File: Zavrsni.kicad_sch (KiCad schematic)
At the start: 8 parts, among them J1 JOYSTICK, J2 LSM6DS3, J3 ILI9341, J4 NUCLEO-H743ZI2, J5 NUCLEO-H743ZI2, J6 NUCLEO-H743ZI2, J7 NUCLEO-H743ZI2, K1 JST-2pin-SMD

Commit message: Add files via upload
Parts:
- added C1: 100 nF, Capacitor_SMD:C_0603_1608Metric, symbol Device:C
- added C2, C3, C4, C5: C, Capacitor_SMD:C_0603_1608Metric, symbol Device:C
- added R1, R2, R3, R4, R5, R6: 10k, Resistor_SMD:R_0201_0603Metric, symbol Device:R
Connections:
- net +3V3: now also C1.1, C2.2, C3.2, C4.1, C5.1
- net CS: now also R4.1; no longer J3.3 (Pin_3)
- net GND: now also C1.2, C2.1, C3.1, C4.2, C5.2
- net SCK: now also R1.1; no longer J3.7 (Pin_7)
- net SDI: now also R2.1; no longer J3.6 (Pin_6)
- net SDO(MISO): now also R3.1; no longer J3.9 (Pin_9)
- new net: J3.7 (Pin_7), R1.2
- new net: J3.6 (Pin_6), R2.2
- new net: J3.3 (Pin_3), R4.2
- new net: J3.9 (Pin_9), R3.2
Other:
- moved on the sheet: J3

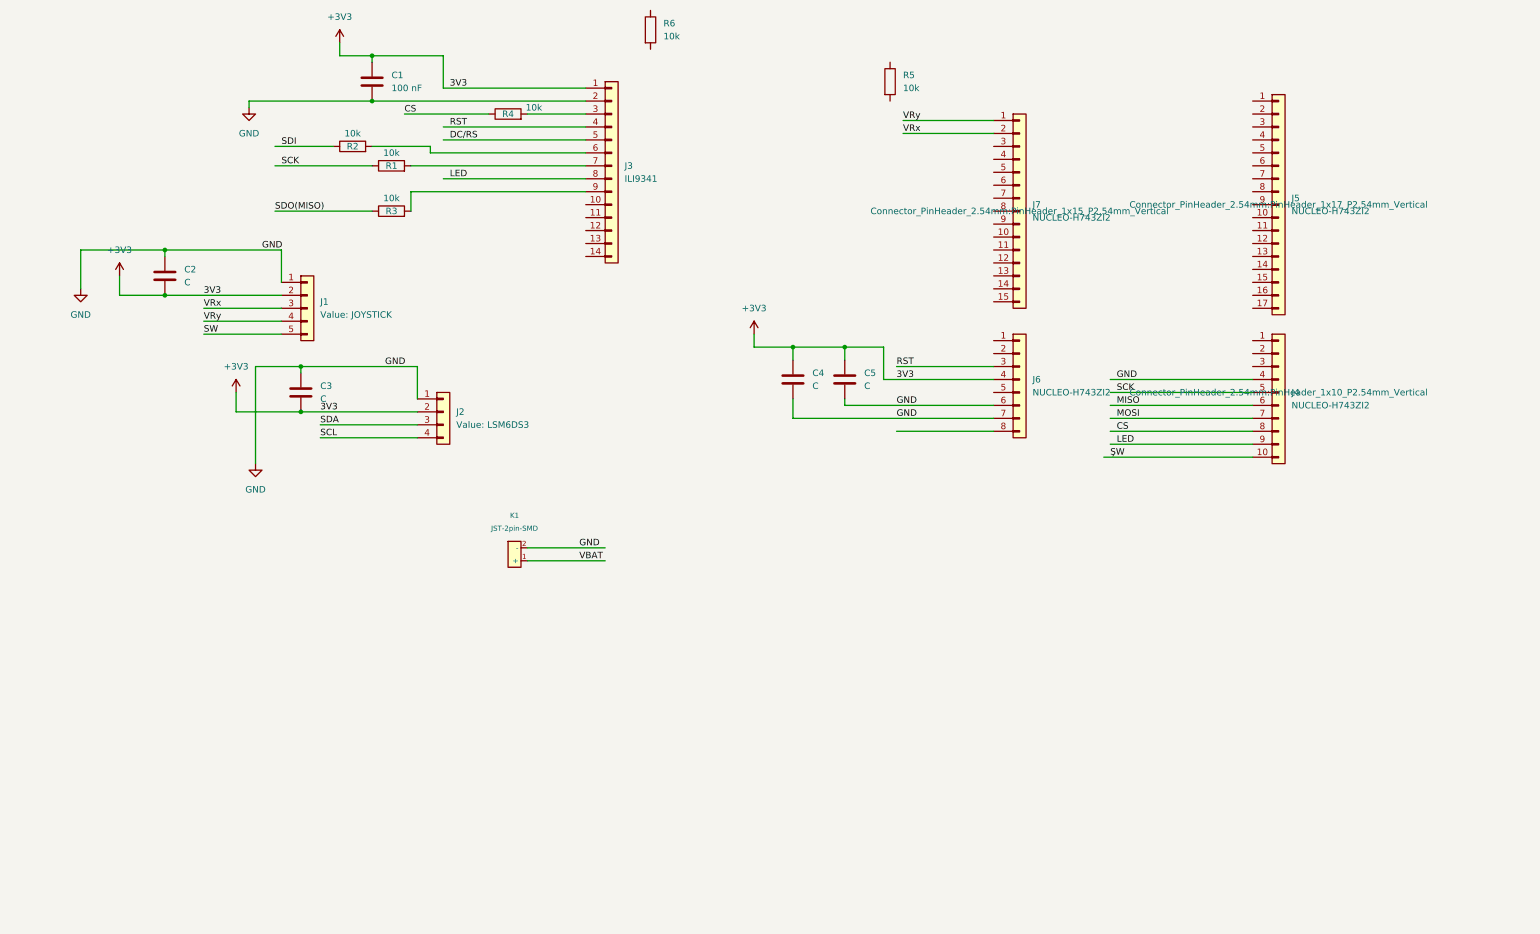
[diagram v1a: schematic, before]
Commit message: Added push buttons, and footprint for JST connector
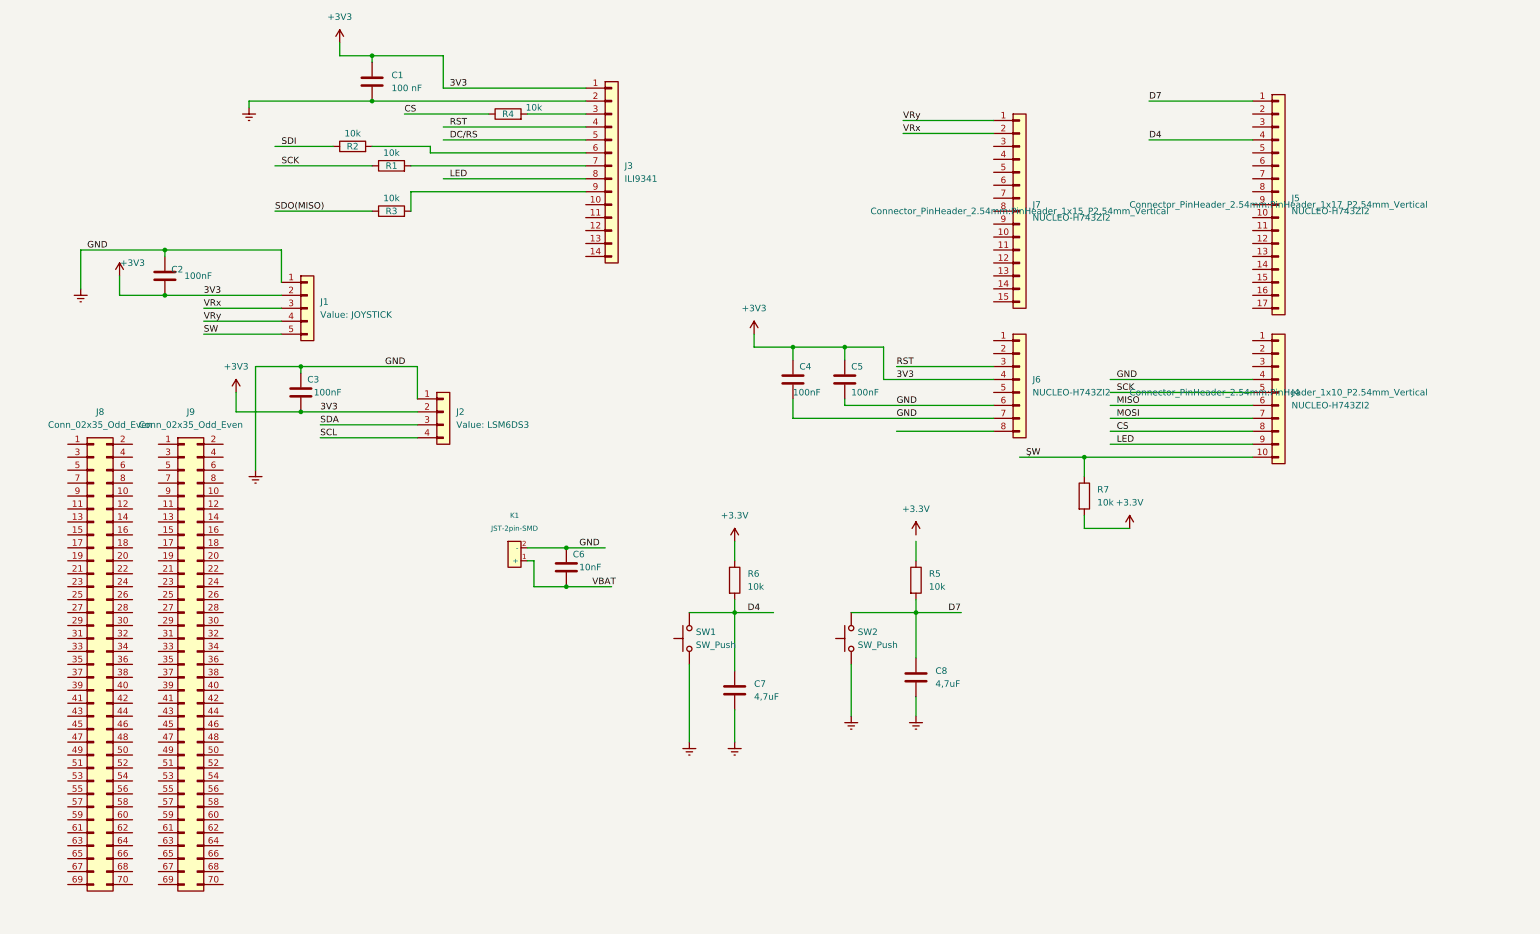
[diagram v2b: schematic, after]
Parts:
- added C6: 10nF, Capacitor_SMD:C_0603_1608Metric, symbol Device:C
- added C7, C8: 4,7uF, Capacitor_SMD:C_0603_1608Metric, symbol Device:C
- added J8, J9: Conn_02x35_Odd_Even, Connector_PinHeader_2.54mm:PinHeader_2x35_P2.54mm_Vertical, symbol Connector_Generic:Conn_02x35_Odd_Even
- added R7: 10k, Resistor_SMD:R_0603_1608Metric, symbol Device:R
- added SW1, SW2: SW_Push, Button_Switch_SMD:SW_Push_1P1T_NO_6x6mm_H9.5mm, symbol Switch:SW_Push
- C2, C3, C4, C5: value C -> 100nF
- K1: footprint e-radionica.com footprinti:JST-2pin-SMD -> JST conector:jst connector
- R1, R2, R3, R4: footprint Resistor_SMD:R_0201_0603Metric -> Resistor_SMD:R_0603_1608Metric
- R5, R6: footprint Resistor_SMD:R_0201_0603Metric -> Capacitor_SMD:C_0603_1608Metric
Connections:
- net VBAT: now also C6.2
- net ŞW: now also R7.1
- net +3.3V: now reaches R6.1
- net +3.3V: now also R7.2
- net D4: now reaches R6.2
- net D4: now also J5.4 (Pin_4), C7.1, SW1.2
- net D7: now reaches R5.2
- net D7: now also J5.1 (Pin_1), C8.1, SW2.2
- net GND renamed Earth
- net Earth: now also C6.1, C7.2, C8.2, SW1.1, SW2.1
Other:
- moved on the sheet: R5, R6

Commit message: Add files via upload
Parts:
- added C10, C11, C9: 10nF, Capacitor_SMD:C_0603_1608Metric, symbol Device:C
- added C12: 10uF, Capacitor_SMD:C_0603_1608Metric, symbol Device:C
- added Q1: NMOS, symbol Simulation_SPICE:NMOS
- added R10, R12, R13, R8, R9: 100R, Resistor_SMD:R_0603_1608Metric, symbol Device:R
- added R11: 10k, Resistor_SMD:R_0603_1608Metric, symbol Device:R
- C6: value 10nF -> 10uF
- C7, C8: value 4,7uF -> 10nF
- R1, R2, R3, R4: value 10k -> 330R
- R7: value 10k -> R; footprint Resistor_SMD:R_0603_1608Metric -> (none)
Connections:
- net +3.3V: no longer R7.2
- net CS: no longer J4.8 (Pin_8)
- net D4: now also R13.2; no longer SW1.2
- net D7: now also R12.2; no longer SW2.2
- net DC/RS: now also J4.8 (Pin_8)
- net Earth: now also R7.2, C10.2, C11.2, C12.1, C9.2, Q1.3 (S)
- net RST: no longer J3.4 (Pin_4)
- net SCL: now also J4.1 (Pin_1)
- net SDA: now also J4.2 (Pin_2)
- net SW: now also J4.10 (Pin_10), C11.1, R10.2, R11.2; no longer J1.5 (Pin_5)
- net VRx: now also C9.1, R8.1; no longer J1.3 (Pin_3)
- net VRy: no longer J1.4 (Pin_4)
- net VBAT renamed VCC
- net VCC: now also C12.2, R11.1
- net ŞW: no longer names the net of R7.1
- net ŞW: now also Q1.2 (G); no longer J4.10 (Pin_10)
- new net: C10.1, R9.1
- new net: J1.4 (Pin_4), R9.2
- new net: J1.3 (Pin_3), R8.2
- new net: J1.5 (Pin_5), R10.1
- new net: R12.1, SW2.2
- new net: R13.1, SW1.2
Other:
- moved on the sheet: C3, C6, J2, J8, J9, K1

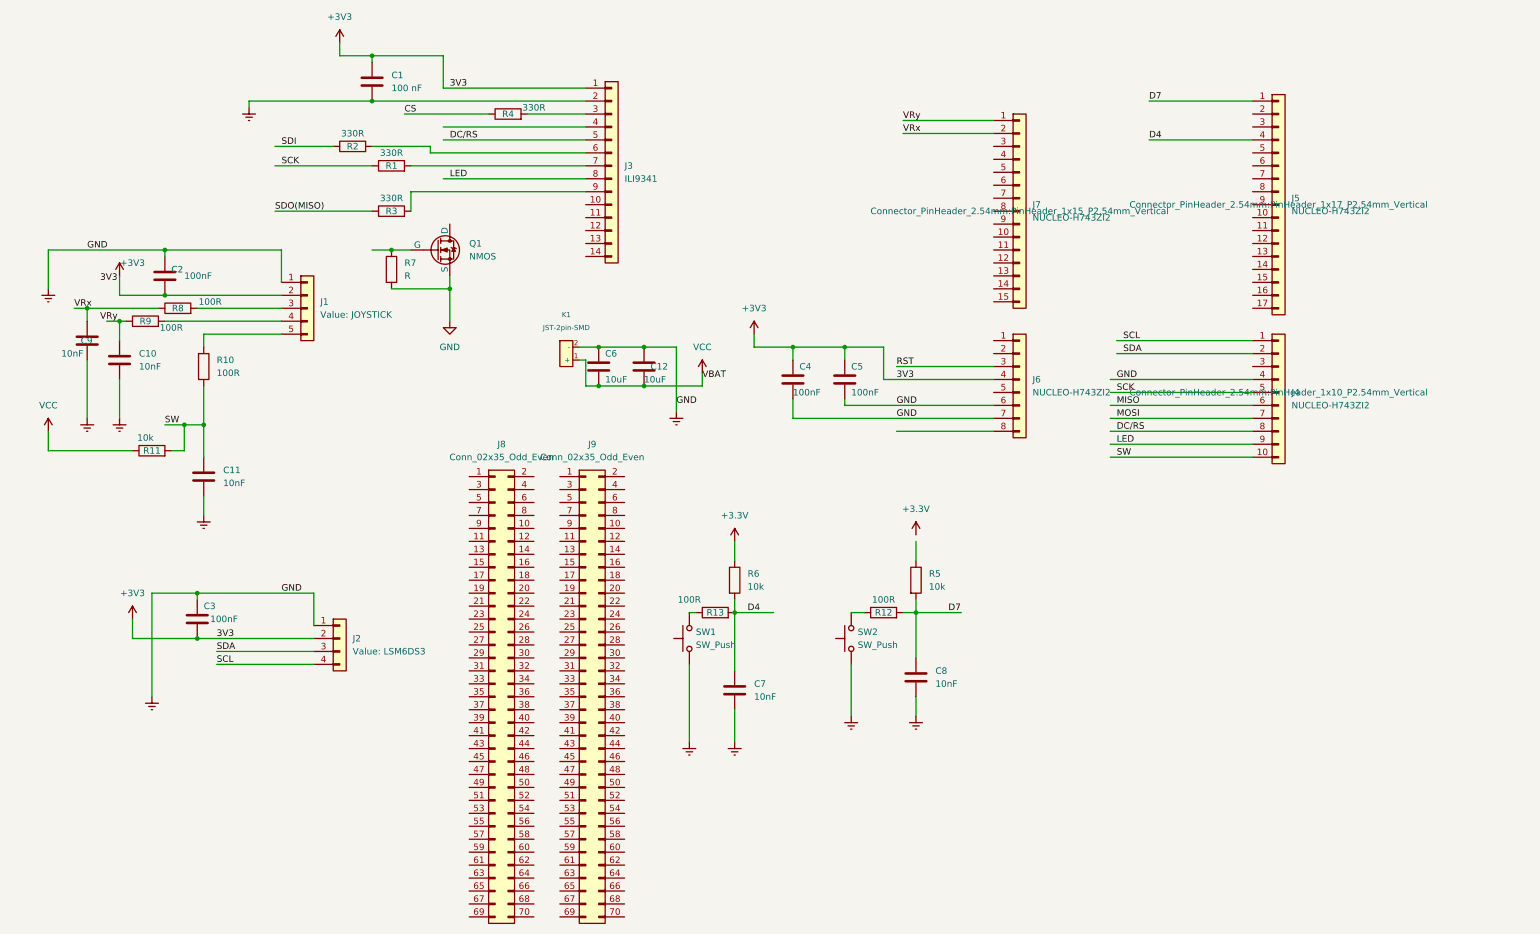
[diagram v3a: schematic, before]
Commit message: Start connecting the lines on the pcb
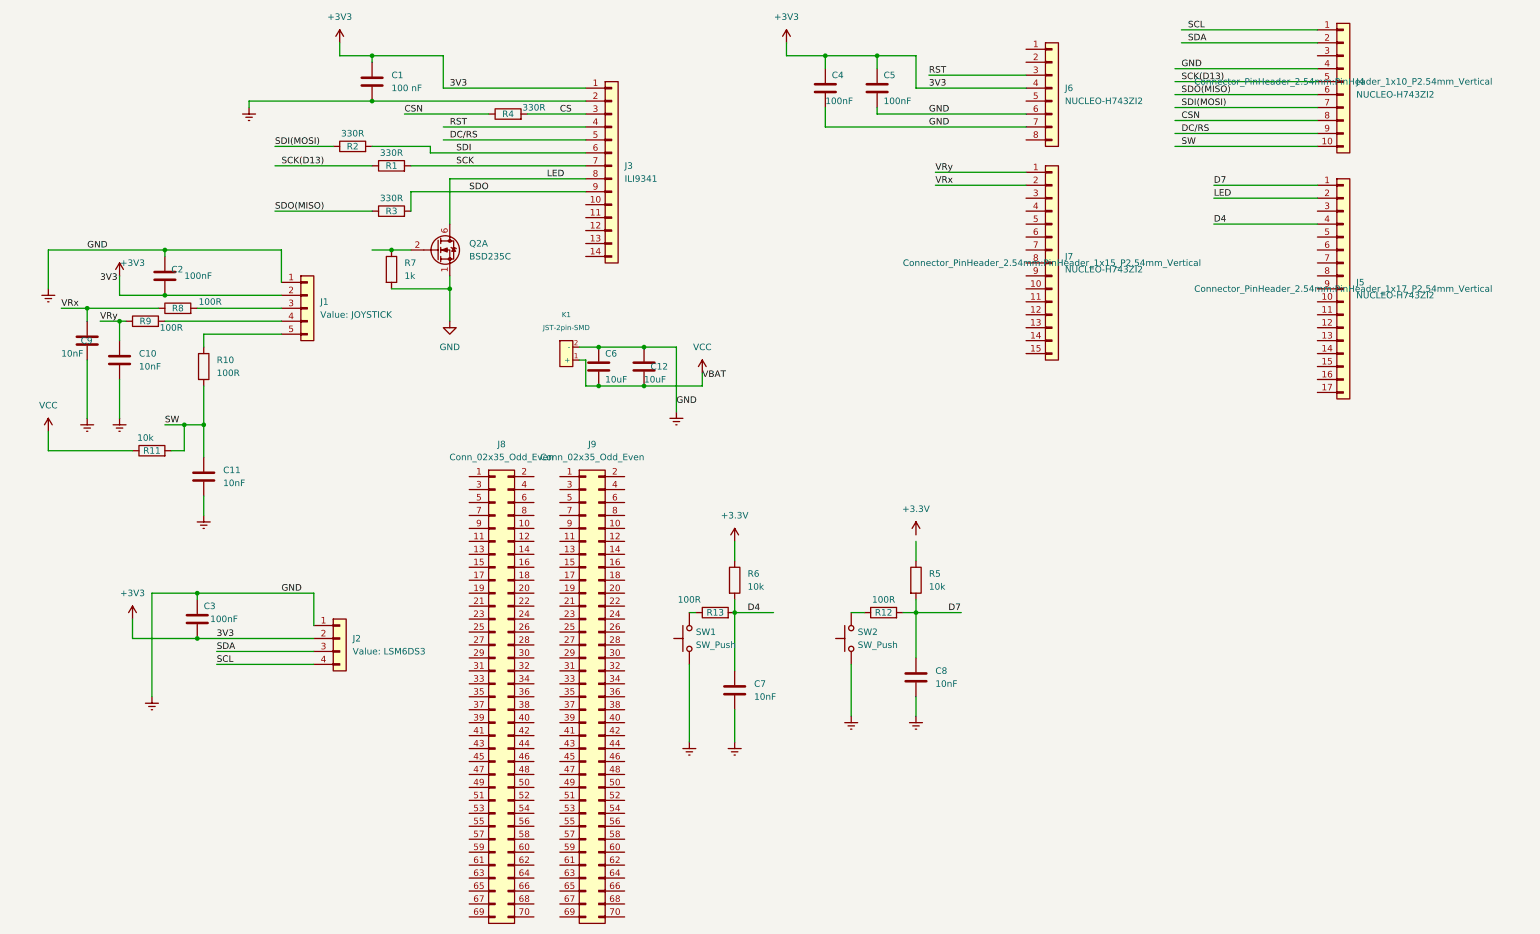
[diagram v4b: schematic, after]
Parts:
- removed Q1: NMOS, symbol Simulation_SPICE:NMOS
- added Q2: BSD235C, Package_TO_SOT_SMD:SOT-363_SC-70-6, symbol Transistor_FET:BSD235C
- R7: value R -> 1k; footprint (none) -> Resistor_SMD:R_0603_1608Metric
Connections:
- net MISO is gone; now on net SDO(MISO): J4.6 (Pin_6)
- net CS: now also J3.3 (Pin_3), R4.2; no longer R4.1
- net DC/RS: now also J4.9 (Pin_9); no longer J4.8 (Pin_8)
- net Earth: now also Q2.1 (SN)
- net LED: now also J5.2 (Pin_2), Q2.6 (DN); no longer J4.9 (Pin_9)
- net RST: now also J3.4 (Pin_4)
- net SCK: now also J3.7 (Pin_7), R1.2; no longer J4.5 (Pin_5), R1.1
- net SDI: now also J3.6 (Pin_6), R2.2; no longer R2.1
- net VRy: now also C10.1, R9.1
- net at R7.1: now also Q2.2 (GN)
- net SDO: now reaches J3.9 (Pin_9), R3.2
- net MOSI renamed SDI(MOSI)
- net SDI(MOSI): now also R2.1
- new net CSN: J4.8 (Pin_8), R4.1
- new net SCK(D13): J4.5 (Pin_5), R1.1
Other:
- moved on the sheet: C4, C5, J4, J5, J6, J7

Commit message: Add files via upload
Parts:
- removed J1: JOYSTICK, Connector_PinSocket_2.54mm:PinSocket_1x05_P2.54mm_Vertical, symbol Connector_Generic:Conn_01x05
- removed J2: LSM6DS3, Connector_PinSocket_2.54mm:PinSocket_1x04_P2.54mm_Vertical, symbol Connector_Generic:Conn_01x04
- removed J3: ILI9341, Connector_PinSocket_2.54mm:PinSocket_1x14_P2.54mm_Vertical, symbol Connector_Generic:Conn_01x14
- removed J4: NUCLEO-H743ZI2, Connector_PinHeader_2.54mm:PinHeader_1x10_P2.54mm_Vertical, symbol Connector_Generic:Conn_01x10
- removed J5: NUCLEO-H743ZI2, Connector_PinHeader_2.54mm:PinHeader_1x17_P2.54mm_Vertical, symbol Connector_Generic:Conn_01x17
- removed J6: NUCLEO-H743ZI2, Connector_PinHeader_2.54mm:PinHeader_1x08_P2.54mm_Vertical, symbol Connector_Generic:Conn_01x08
- removed J7: NUCLEO-H743ZI2, Connector_PinHeader_2.54mm:PinHeader_1x15_P2.54mm_Vertical, symbol Connector_Generic:Conn_01x15
- removed J8, J9: Conn_02x35_Odd_Even, Connector_PinHeader_2.54mm:PinHeader_2x35_P2.54mm_Vertical, symbol Connector_Generic:Conn_02x35_Odd_Even
- removed Q2: BSD235C, Package_TO_SOT_SMD:SOT-363_SC-70-6, symbol Transistor_FET:BSD235C
- removed R7: 1k, Resistor_SMD:R_0603_1608Metric, symbol Device:R
- added DISP1: LCD TFT ILI9341, BornaKiCad:LCD_TFT_2.4, symbol BornaLibrary:LCD_TFT_2.4
- added JOYSTICK_HW_1: ~, JOYSTICK:JOYSTICK, symbol joystick_symbol1:JOYSTICK-HW-504
- added LSM6DS1: ~, LSMDS3_akceleometar_žiroskop:LSM6DS3, symbol LSM6DS3_symbol:LSM6DS3
- added NMOS2: ~, Package_TO_SOT_SMD:SOT-23-3, symbol NMOS_symbol:NMOS
- added NUCLEO_144_H743ZI2: ~, NUCLEO_PCB:NUCLEO_PCB, symbol NUCLEO_SYMBOL:NUCLEO_144
- added PMOS1: ~, Package_TO_SOT_SMD:SOT-23-3, symbol PMOS_symbol:PMOS
- added R14, R15: 4,7k, Resistor_SMD:R_0603_1608Metric, symbol Device:R
- added R16, R17: 10k, symbol Device:R
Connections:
- net +3V3: now also R11.2, DISP1.1 (VCC), JOYSTICK_HW_1.2 (3V3), LSM6DS1.2 (INT2), NMOS2. (S), NUCLEO_144_H743ZI2.1 (SCL), NUCLEO_144_H743ZI2.2 (SDA), NUCLEO_144_H743ZI2.4 (GND), PMOS1. (S), R14.1, R15.1, R16.1
- net CS: now also DISP1.3 (CS)
- net CSN: now also NUCLEO_144_H743ZI2.8 (VIN)
- net D4: now also NUCLEO_144_H743ZI2.14 (D4(PWM))
- net D7: now also NUCLEO_144_H743ZI2.11 (D7(PWM))
- net DC/RS: now also DISP1.5 (D/C), NUCLEO_144_H743ZI2.9 (PWM)
- net Earth: now also DISP1.2 (GND), JOYSTICK_HW_1.1 (GND), LSM6DS1.1 (INT1), NMOS2. (S), NUCLEO_144_H743ZI2.4 (GND), NUCLEO_144_H743ZI2.6 (MISO), NUCLEO_144_H743ZI2.7 (MOSI), R17.1
- net LED: now also DISP1.8 (LED), PMOS1. (S)
- net RST: now also DISP1.4 (RESET), NUCLEO_144_H743ZI2.3 (NRST)
- net SCK: now also R1.1, DISP1.7 (SCK); no longer R1.2
- net SCK(D13): now also R1.2, NUCLEO_144_H743ZI2.5 (SCK); no longer R1.1
- net SDI: now also R2.1, DISP1.6 (MOSI); no longer R2.2
- net SDI(MOSI): now also R2.2, NUCLEO_144_H743ZI2.7 (MOSI); no longer R2.1
- net SDO: now also DISP1.9 (MISO)
- net SW: now also R10.1, R11.1, NUCLEO_144_H743ZI2.10 (D8); no longer R10.2, R11.2
- net VCC: no longer R11.1
- net VRx: now also R8.2, NUCLEO_144_H743ZI2.10 (D8); no longer R8.1
- net VRy: now also NUCLEO_144_H743ZI2.9 (PWM)
- net at R9.2: now also JOYSTICK_HW_1.4 (VRy)
- new net: LSM6DS1.4 (SCL), R15.2
- new net: PMOS1. (S), R16.2
- new net: LSM6DS1.3 (SDA), R14.2
- new net: JOYSTICK_HW_1.3 (VRx), R8.1
- new net: JOYSTICK_HW_1.5 (SW), R10.2
- new net LED(PWM): NMOS2. (S), NUCLEO_144_H743ZI2.12 (D6(PWM)), R17.2
- new net SD0(MISO): NUCLEO_144_H743ZI2.6 (MISO)
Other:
- moved on the sheet: C1, C10, C11, C12, C2, C3, C4, C5, C6, C7, C8, C9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

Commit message: Add files via upload
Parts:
- R16, R17: footprint (none) -> Resistor_SMD:R_0603_1608Metric
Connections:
- net VCC is gone; now on net +3.3V: C12.2, C6.2, K1.1 (+)
- net +3.3V: now also C1.1, C2.2, C3.2, C4.1, C5.1, DISP1.1 (VCC), JOYSTICK_HW_1.2 (3V3), LSM6DS1.2 (3V3), NUCLEO_144_H743ZI2.7 (3V3), PMOS1.1 (S), R11.2, R16.1, R5.1
- net CSN: now also NUCLEO_144_H743ZI2.62 (CS); no longer NUCLEO_144_H743ZI2.8 (VIN)
- net D4: now also NUCLEO_144_H743ZI2.74 (D4(PWM)); no longer NUCLEO_144_H743ZI2.14 (D4(PWM))
- net D7: now also NUCLEO_144_H743ZI2.68 (D7(PWM)); no longer NUCLEO_144_H743ZI2.11 (D7(PWM))
- net DC/RS: now also NUCLEO_144_H743ZI2.64 (PWM); no longer NUCLEO_144_H743ZI2.9 (PWM)
- net Earth: now also NMOS2.3 (S), NUCLEO_144_H743ZI2.11 (GND), NUCLEO_144_H743ZI2.13 (GND), NUCLEO_144_H743ZI2.54 (GND); no longer NMOS2. (S), NUCLEO_144_H743ZI2.4 (GND), NUCLEO_144_H743ZI2.6 (MISO), NUCLEO_144_H743ZI2.7 (MOSI)
- net LED: now also PMOS1.3 (D); no longer PMOS1. (S)
- net LED(PWM): now also NMOS2.2 (G), NUCLEO_144_H743ZI2.70 (D6(PWM)); no longer NMOS2. (S), NUCLEO_144_H743ZI2.12 (D6(PWM))
- net SCK(D13): now also NUCLEO_144_H743ZI2.56 (SCK); no longer NUCLEO_144_H743ZI2.5 (SCK)
- net SDI(MOSI): now also NUCLEO_144_H743ZI2.60 (MOSI); no longer NUCLEO_144_H743ZI2.7 (MOSI)
- net SDO(MISO): now also NUCLEO_144_H743ZI2.58 (MISO)
- net SW: now also NUCLEO_144_H743ZI2.66 (D8); no longer NUCLEO_144_H743ZI2.10 (D8)
- net VRx: no longer NUCLEO_144_H743ZI2.10 (D8)
- net VRy: no longer NUCLEO_144_H743ZI2.9 (PWM)
- net D: now reaches R16.2
- net D: now also NMOS2.1 (D), PMOS1.2 (G); no longer PMOS1. (S)
- net NC: now reaches NUCLEO_144_H743ZI2.1 (NC)
- net A0: now reaches NUCLEO_144_H743ZI2.17 (A0)
- net REF: now reaches NUCLEO_144_H743ZI2.3 (REF)
- net NRST: now reaches NUCLEO_144_H743ZI2.5 (NRST)
- net NRST: now also DISP1.4 (RESET)
- removed net +3V3: C1.1, C2.2, C3.2, C4.1, C5.1, DISP1.1 (VCC), JOYSTICK_HW_1.2 (3V3), LSM6DS1.2 (INT2), NMOS2. (S), NUCLEO_144_H743ZI2.1 (SCL), NUCLEO_144_H743ZI2.2 (SDA), NUCLEO_144_H743ZI2.4 (GND), PMOS1. (S), R11.2, R14.1, R15.1, R16.1
- removed net RST: DISP1.4 (RESET), NUCLEO_144_H743ZI2.3 (NRST)
- removed net SD0(MISO): NUCLEO_144_H743ZI2.6 (MISO)
- new net A1: NUCLEO_144_H743ZI2.19 (A1)
- new net SCL: NUCLEO_144_H743ZI2.48 (SCL), R15.1
- new net SDA: NUCLEO_144_H743ZI2.50 (SDA), R14.1
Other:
- moved on the sheet: C1, C10, C11, C2, C3, C7, C8, C9, DISP1, JOYSTICK_HW_1, LSM6DS1, R1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

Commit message: Add files via upload
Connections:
- net A0 is gone; now on net VRx: NUCLEO_144_H743ZI2.17 (A0)
- net A1 is gone; now on net VRy: NUCLEO_144_H743ZI2.19 (A1)
- net SCL is gone; now on net +3.3V: NUCLEO_144_H743ZI2.48 (SCL), R15.1
- net SDA is gone; now on net +3.3V: NUCLEO_144_H743ZI2.50 (SDA), R14.1
- net dirY: now reaches JOYSTICK_HW_1.4 (VRy), R9.2
- net dirX: now reaches JOYSTICK_HW_1.3 (VRx), R8.1
- net T1: now reaches JOYSTICK_HW_1.5 (SW), R10.2
